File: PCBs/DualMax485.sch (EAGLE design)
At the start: 10 parts, among them IC2 7805DT, J1 6V-12V

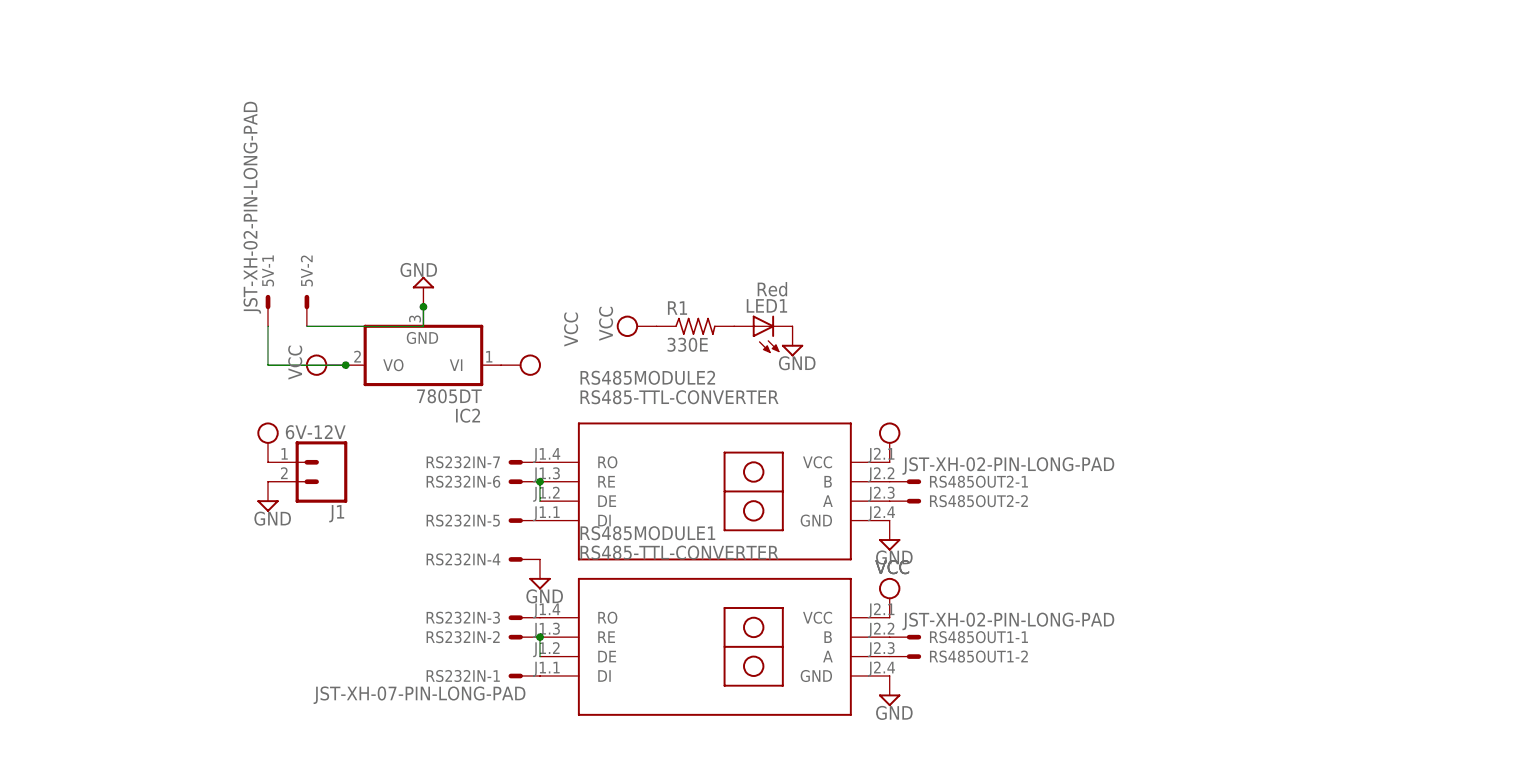
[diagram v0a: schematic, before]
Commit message: resistors added to max485
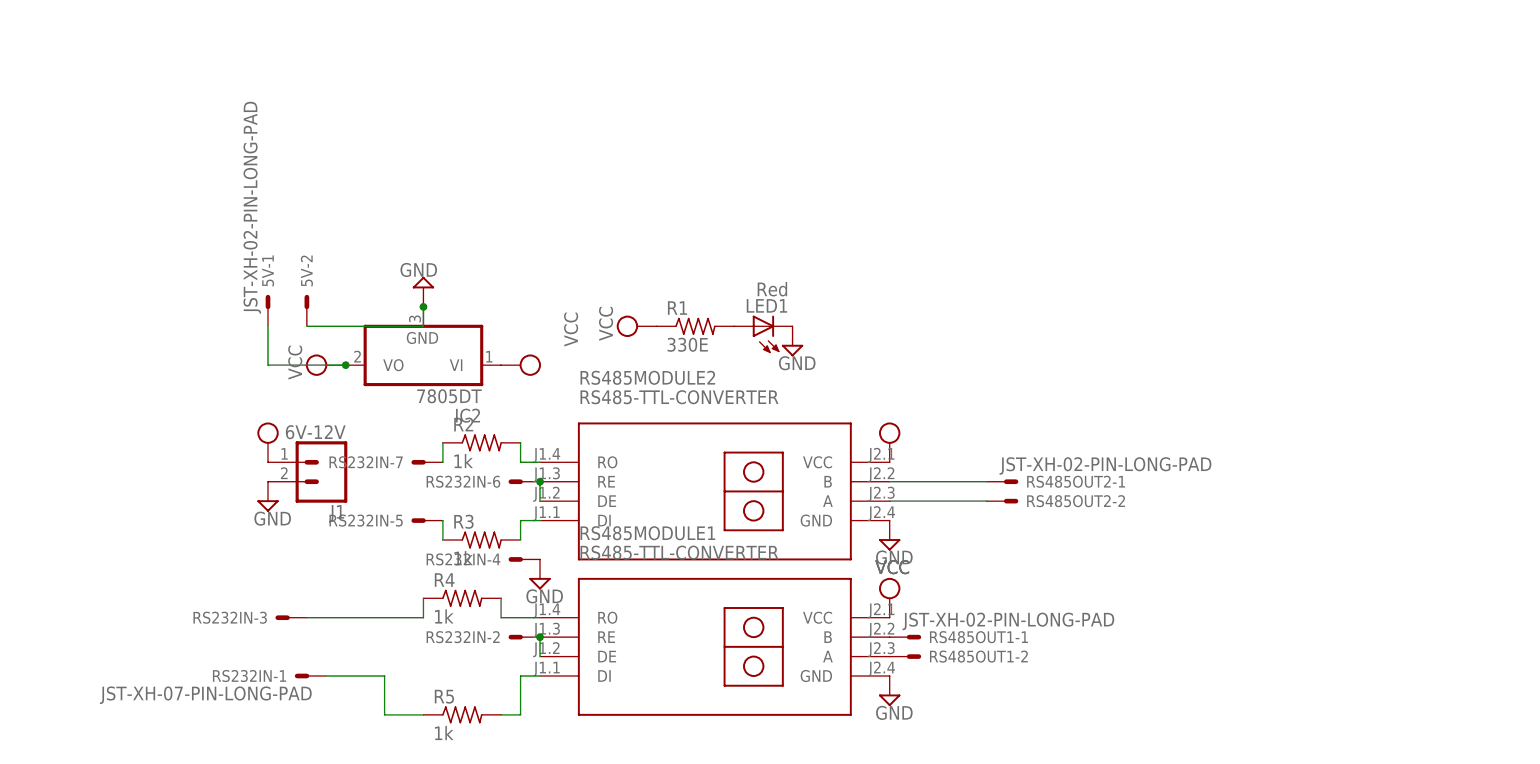
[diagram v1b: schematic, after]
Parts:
- added R2, R3, R4, R5: 1k, adafruit:R-US_M0805
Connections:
- new net N$11: R2.1, RS232IN-7.S
- new net N$14: R4.2, RS485MODULE1.RO
- new net N$15: R5.2, RS485MODULE1.DI
- new net N$5: R3.1, RS232IN-5.S
- net N$10: now also R4.1; no longer RS485MODULE1.RO
- net N$2: now also R3.2; no longer RS232IN-5.S
- net N$3: now also R2.2; no longer RS232IN-7.S
- net N$8: now also R5.1; no longer RS485MODULE1.DI
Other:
- moved on the sheet: RS232IN-1, RS232IN-3, RS232IN-5, RS232IN-7, RS485OUT2-1, RS485OUT2-2
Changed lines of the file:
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@@
 <part name="RS485MODULE1" library="diy-modules" deviceset="RS485-TTL-CONVERTER" device=""/>
 <part name="5V" library="Rembrandt Electronics - JST XH Connectors v1-0" deviceset="JST-XH-02-PIN" device="-LONG-PAD"/>
+<part name="R2" library="adafruit" deviceset="R-US_" device="M0805" value="1k"/>
+<part name="R3" library="adafruit" deviceset="R-US_" device="M0805" value="1k"/>
+<part name="R4" library="adafruit" deviceset="R-US_" device="M0805" value="1k"/>
+<part name="R5" library="adafruit" deviceset="R-US_" device="M0805" value="1k"/>
 </parts>
 <sheets>
@@
 <attribute name="VALUE" x="-37.465" y="116.205" size="1.778" layer="96"/>
 </instance>
-<instance part="RS232IN" gate="-1" x="-71.12" y="76.2" smashed="yes" rot="R180">
-<attribute name="NAME" x="-73.66" y="76.962" size="1.524" layer="95" rot="R180"/>
-<attribute name="VALUE" x="-70.358" y="74.803" size="1.778" layer="96" rot="R180"/>
+<instance part="RS232IN" gate="-1" x="-99.06" y="76.2" smashed="yes" rot="R180">
+<attribute name="NAME" x="-101.6" y="76.962" size="1.524" layer="95" rot="R180"/>
+<attribute name="VALUE" x="-98.298" y="74.803" size="1.778" layer="96" rot="R180"/>
 </instance>
 <instance part="RS232IN" gate="-2" x="-71.12" y="81.28" smashed="yes" rot="R180">
 <attribute name="NAME" x="-73.66" y="82.042" size="1.524" layer="95" rot="R180"/>
 </instance>
-<instance part="RS232IN" gate="-3" x="-71.12" y="83.82" smashed="yes" rot="R180">
-<attribute name="NAME" x="-73.66" y="84.582" size="1.524" layer="95" rot="R180"/>
+<instance part="RS232IN" gate="-3" x="-101.6" y="83.82" smashed="yes" rot="R180">
+<attribute name="NAME" x="-104.14" y="84.582" size="1.524" layer="95" rot="R180"/>
 </instance>
 <instance part="RS232IN" gate="-4" x="-71.12" y="91.44" smashed="yes" rot="R180">
 <attribute name="NAME" x="-73.66" y="92.202" size="1.524" layer="95" rot="R180"/>
 </instance>
-<instance part="RS232IN" gate="-5" x="-71.12" y="96.52" smashed="yes" rot="R180">
-<attribute name="NAME" x="-73.66" y="97.282" size="1.524" layer="95" rot="R180"/>
+<instance part="RS232IN" gate="-5" x="-83.82" y="96.52" smashed="yes" rot="R180">
+<attribute name="NAME" x="-86.36" y="97.282" size="1.524" layer="95" rot="R180"/>
 </instance>
 <instance part="RS232IN" gate="-6" x="-71.12" y="101.6" smashed="yes" rot="R180">
 <attribute name="NAME" x="-73.66" y="102.362" size="1.524" layer="95" rot="R180"/>
 </instance>
-<instance part="RS232IN" gate="-7" x="-71.12" y="104.14" smashed="yes" rot="R180">
-<attribute name="NAME" x="-73.66" y="104.902" size="1.524" layer="95" rot="R180"/>
+<instance part="RS232IN" gate="-7" x="-83.82" y="104.14" smashed="yes" rot="R180">
+<attribute name="NAME" x="-86.36" y="104.902" size="1.524" layer="95" rot="R180"/>
 </instance>
 <instance part="SUPPLY17" gate="GND" x="-68.58" y="88.9" smashed="yes">
@@
 <attribute name="VALUE" x="-21.082" y="82.677" size="1.778" layer="96"/>
 </instance>
-<instance part="RS485OUT2" gate="-2" x="-20.32" y="99.06" smashed="yes">
-<attribute name="NAME" x="-17.78" y="98.298" size="1.524" layer="95"/>
-</instance>
-<instance part="RS485OUT2" gate="-1" x="-20.32" y="101.6" smashed="yes">
-<attribute name="NAME" x="-17.78" y="100.838" size="1.524" layer="95"/>
-<attribute name="VALUE" x="-21.082" y="102.997" size="1.778" layer="96"/>
+<instance part="RS485OUT2" gate="-2" x="-7.62" y="99.06" smashed="yes">
+<attribute name="NAME" x="-5.08" y="98.298" size="1.524" layer="95"/>
+</instance>
+<instance part="RS485OUT2" gate="-1" x="-7.62" y="101.6" smashed="yes">
+<attribute name="NAME" x="-5.08" y="100.838" size="1.524" layer="95"/>
+<attribute name="VALUE" x="-8.382" y="102.997" size="1.778" layer="96"/>
 </instance>
 <instance part="IC2" gate="A1" x="-83.82" y="116.84" smashed="yes" rot="R180">
@@
 <attribute name="NAME" x="-103.378" y="127" size="1.524" layer="95" rot="R90"/>
 <attribute name="VALUE" x="-105.537" y="123.698" size="1.778" layer="96" rot="R90"/>
+</instance>
+<instance part="R2" gate="G$1" x="-76.2" y="106.68" smashed="yes">
+<attribute name="NAME" x="-80.01" y="108.1786" size="1.778" layer="95"/>
+<attribute name="VALUE" x="-80.01" y="103.378" size="1.778" layer="96"/>
+</instance>
+<instance part="R3" gate="G$1" x="-76.2" y="93.98" smashed="yes">
+<attribute name="NAME" x="-80.01" y="95.4786" size="1.778" layer="95"/>
+<attribute name="VALUE" x="-80.01" y="90.678" size="1.778" layer="96"/>
+</instance>
+<instance part="R4" gate="G$1" x="-78.74" y="86.36" smashed="yes">
+<attribute name="NAME" x="-82.55" y="87.8586" size="1.778" layer="95"/>
+<attribute name="VALUE" x="-82.55" y="83.058" size="1.778" layer="96"/>
+</instance>
+<instance part="R5" gate="G$1" x="-78.74" y="71.12" smashed="yes">
+<attribute name="NAME" x="-82.55" y="72.6186" size="1.778" layer="95"/>
+<attribute name="VALUE" x="-82.55" y="67.818" size="1.778" layer="96"/>
 </instance>
 </instances>
@@
 <net name="N$2" class="0">
 <segment>
-<pinref part="RS232IN" gate="-5" pin="S"/>
 <pinref part="RS485MODULE2" gate="G$1" pin="DI"/>
+<pinref part="R3" gate="G$1" pin="2"/>
+<wire x1="-71.12" y1="96.52" x2="-68.58" y2="96.52" width="0.1524" layer="91"/>
+<wire x1="-71.12" y1="96.52" x2="-71.12" y2="93.98" width="0.1524" layer="91"/>
 </segment>
 </net>
 <net name="N$3" class="0">
 <segment>
-<pinref part="RS232IN" gate="-7" pin="S"/>
 <pinref part="RS485MODULE2" gate="G$1" pin="RO"/>
+<wire x1="-71.12" y1="104.14" x2="-68.58" y2="104.14" width="0.1524" layer="91"/>
+<pinref part="R2" gate="G$1" pin="2"/>
+<wire x1="-71.12" y1="106.68" x2="-71.12" y2="104.14" width="0.1524" layer="91"/>
 </segment>
 </net>
@@
 <pinref part="RS485MODULE2" gate="G$1" pin="B"/>
 <pinref part="RS485OUT2" gate="-1" pin="S"/>
+<wire x1="-10.16" y1="101.6" x2="-22.86" y2="101.6" width="0.1524" layer="91"/>
 </segment>
 </net>
@@
 <pinref part="RS485MODULE2" gate="G$1" pin="A"/>
 <pinref part="RS485OUT2" gate="-2" pin="S"/>
+<wire x1="-10.16" y1="99.06" x2="-22.86" y2="99.06" width="0.1524" layer="91"/>
 </segment>
 </net>
@@
 <segment>
 <pinref part="RS232IN" gate="-1" pin="S"/>
-<pinref part="RS485MODULE1" gate="G$1" pin="DI"/>
+<wire x1="-96.52" y1="76.2" x2="-88.9" y2="76.2" width="0.1524" layer="91"/>
+<pinref part="R5" gate="G$1" pin="1"/>
+<wire x1="-83.82" y1="71.12" x2="-88.9" y2="71.12" width="0.1524" layer="91"/>
+<wire x1="-88.9" y1="71.12" x2="-88.9" y2="76.2" width="0.1524" layer="91"/>
 </segment>
 </net>
@@
 <segment>
 <pinref part="RS232IN" gate="-3" pin="S"/>
-<pinref part="RS485MODULE1" gate="G$1" pin="RO"/>
+<wire x1="-99.06" y1="83.82" x2="-83.82" y2="83.82" width="0.1524" layer="91"/>
+<pinref part="R4" gate="G$1" pin="1"/>
+<wire x1="-83.82" y1="86.36" x2="-83.82" y2="83.82" width="0.1524" layer="91"/>
 </segment>
 </net>
@@
 </segment>
 </net>
+<net name="N$5" class="0">
+<segment>
+<pinref part="R3" gate="G$1" pin="1"/>
+<pinref part="RS232IN" gate="-5" pin="S"/>
+<wire x1="-81.28" y1="96.52" x2="-81.28" y2="93.98" width="0.1524" layer="91"/>
+</segment>
+</net>
+<net name="N$11" class="0">
+<segment>
+<pinref part="RS232IN" gate="-7" pin="S"/>
+<pinref part="R2" gate="G$1" pin="1"/>
+<wire x1="-81.28" y1="106.68" x2="-81.28" y2="104.14" width="0.1524" layer="91"/>
+</segment>
+</net>
+<net name="N$15" class="0">
+<segment>
+<pinref part="RS485MODULE1" gate="G$1" pin="DI"/>
+<wire x1="-71.12" y1="76.2" x2="-68.58" y2="76.2" width="0.1524" layer="91"/>
+<pinref part="R5" gate="G$1" pin="2"/>
+<wire x1="-73.66" y1="71.12" x2="-71.12" y2="71.12" width="0.1524" layer="91"/>
+<wire x1="-71.12" y1="71.12" x2="-71.12" y2="76.2" width="0.1524" layer="91"/>
+</segment>
+</net>
+<net name="N$14" class="0">
+<segment>
+<pinref part="RS485MODULE1" gate="G$1" pin="RO"/>
+<wire x1="-73.66" y1="83.82" x2="-68.58" y2="83.82" width="0.1524" layer="91"/>
+<pinref part="R4" gate="G$1" pin="2"/>
+<wire x1="-73.66" y1="86.36" x2="-73.66" y2="83.82" width="0.1524" layer="91"/>
+</segment>
+</net>

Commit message: updated board
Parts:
- removed RS485OUT1, RS485OUT2: JST-XH-02-PIN-LONG-PAD, Rembrandt Electronics - JST XH Connectors v1-0:JST-XH-02-PIN-LONG-PAD
- added RS485CONNECTEDTOD-D+GND, RS485OUTCONNECTEDTOD-D+GND: JST-XH-03-PIN-LONG-PAD, Rembrandt Electronics - JST XH Connectors v1-0:JST-XH-03-PIN-LONG-PAD
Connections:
- net GND: now also RS485CONNECTEDTOD-D+GND-3.S, RS485OUTCONNECTEDTOD-D+GND-3.S
- net N$12: now also RS485CONNECTEDTOD-D+GND-1.S; no longer RS485OUT1-1.S
- net N$13: now also RS485CONNECTEDTOD-D+GND-2.S; no longer RS485OUT1-2.S
- net N$4: now also RS485OUTCONNECTEDTOD-D+GND-1.S; no longer RS485OUT2-1.S
- net N$6: now also RS485OUTCONNECTEDTOD-D+GND-2.S; no longer RS485OUT2-2.S
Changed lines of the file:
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@@
 <part name="RS232IN" library="Rembrandt Electronics - JST XH Connectors v1-0" deviceset="JST-XH-07-PIN" device="-LONG-PAD"/>
 <part name="SUPPLY17" library="supply2" library_urn="urn:adsk.eagle:library:372" deviceset="GND" device=""/>
-<part name="RS485OUT1" library="Rembrandt Electronics - JST XH Connectors v1-0" deviceset="JST-XH-02-PIN" device="-LONG-PAD"/>
-<part name="RS485OUT2" library="Rembrandt Electronics - JST XH Connectors v1-0" deviceset="JST-XH-02-PIN" device="-LONG-PAD"/>
 <part name="IC2" library="adafruit" deviceset="78*" device="DT" technology="05"/>
 <part name="RS485MODULE2" library="diy-modules" deviceset="RS485-TTL-CONVERTER" device=""/>
@@
 <part name="R4" library="adafruit" deviceset="R-US_" device="M0805" value="1k"/>
 <part name="R5" library="adafruit" deviceset="R-US_" device="M0805" value="1k"/>
+<part name="RS485OUTCONNECTEDTOD-D+GND" library="Rembrandt Electronics - JST XH Connectors v1-0" deviceset="JST-XH-03-PIN" device="-LONG-PAD"/>
+<part name="RS485CONNECTEDTOD-D+GND" library="Rembrandt Electronics - JST XH Connectors v1-0" deviceset="JST-XH-03-PIN" device="-LONG-PAD"/>
 </parts>
 <sheets>
@@
 <attribute name="VALUE" x="-24.765" y="89.535" size="1.778" layer="96"/>
 </instance>
-<instance part="SUPPLY6" gate="GND" x="-22.86" y="73.66" smashed="yes">
-<attribute name="VALUE" x="-24.765" y="70.485" size="1.778" layer="96"/>
+<instance part="SUPPLY6" gate="GND" x="-17.78" y="73.66" smashed="yes">
+<attribute name="VALUE" x="-19.685" y="70.485" size="1.778" layer="96"/>
 </instance>
 <instance part="SUPPLY12" gate="GND" x="-83.82" y="127" smashed="yes" rot="R180">
@@
 <attribute name="VALUE" x="-24.765" y="89.535" size="1.778" layer="96"/>
 </instance>
-<instance part="SUPPLY3" gate="GND" x="-22.86" y="93.98" smashed="yes">
-<attribute name="VALUE" x="-24.765" y="90.805" size="1.778" layer="96"/>
+<instance part="SUPPLY3" gate="GND" x="-15.24" y="93.98" smashed="yes">
+<attribute name="VALUE" x="-17.145" y="90.805" size="1.778" layer="96"/>
 </instance>
 <instance part="SUPPLY1" gate="G$1" x="-96.52" y="116.84" smashed="yes" rot="R90">
@@
 <attribute name="VALUE" x="-70.485" y="85.725" size="1.778" layer="96"/>
 </instance>
-<instance part="RS485OUT1" gate="-2" x="-20.32" y="78.74" smashed="yes">
-<attribute name="NAME" x="-17.78" y="77.978" size="1.524" layer="95"/>
-</instance>
-<instance part="RS485OUT1" gate="-1" x="-20.32" y="81.28" smashed="yes">
-<attribute name="NAME" x="-17.78" y="80.518" size="1.524" layer="95"/>
-<attribute name="VALUE" x="-21.082" y="82.677" size="1.778" layer="96"/>
-</instance>
-<instance part="RS485OUT2" gate="-2" x="-7.62" y="99.06" smashed="yes">
-<attribute name="NAME" x="-5.08" y="98.298" size="1.524" layer="95"/>
-</instance>
-<instance part="RS485OUT2" gate="-1" x="-7.62" y="101.6" smashed="yes">
-<attribute name="NAME" x="-5.08" y="100.838" size="1.524" layer="95"/>
-<attribute name="VALUE" x="-8.382" y="102.997" size="1.778" layer="96"/>
-</instance>
 <instance part="IC2" gate="A1" x="-83.82" y="116.84" smashed="yes" rot="R180">
 <attribute name="NAME" x="-76.2" y="111.125" size="1.778" layer="95" rot="R180"/>
@@
 <attribute name="NAME" x="-82.55" y="72.6186" size="1.778" layer="95"/>
 <attribute name="VALUE" x="-82.55" y="67.818" size="1.778" layer="96"/>
+</instance>
+<instance part="RS485OUTCONNECTEDTOD-D+GND" gate="-1" x="15.24" y="101.6" smashed="yes">
+<attribute name="NAME" x="17.78" y="100.838" size="1.524" layer="95"/>
+<attribute name="VALUE" x="14.478" y="102.997" size="1.778" layer="96"/>
+</instance>
+<instance part="RS485OUTCONNECTEDTOD-D+GND" gate="-2" x="15.24" y="99.06" smashed="yes">
+<attribute name="NAME" x="17.78" y="98.298" size="1.524" layer="95"/>
+</instance>
+<instance part="RS485OUTCONNECTEDTOD-D+GND" gate="-3" x="15.24" y="96.52" smashed="yes">
+<attribute name="NAME" x="17.78" y="95.758" size="1.524" layer="95"/>
+</instance>
+<instance part="RS485CONNECTEDTOD-D+GND" gate="-1" x="15.24" y="83.82" smashed="yes">
+<attribute name="NAME" x="17.78" y="83.058" size="1.524" layer="95"/>
+<attribute name="VALUE" x="14.478" y="85.217" size="1.778" layer="96"/>
+</instance>
+<instance part="RS485CONNECTEDTOD-D+GND" gate="-2" x="15.24" y="81.28" smashed="yes">
+<attribute name="NAME" x="17.78" y="80.518" size="1.524" layer="95"/>
+</instance>
+<instance part="RS485CONNECTEDTOD-D+GND" gate="-3" x="15.24" y="78.74" smashed="yes">
+<attribute name="NAME" x="17.78" y="77.978" size="1.524" layer="95"/>
 </instance>
 </instances>
@@
 <pinref part="RS485MODULE2" gate="G$1" pin="GND"/>
 <pinref part="SUPPLY3" gate="GND" pin="GND"/>
+<pinref part="RS485OUTCONNECTEDTOD-D+GND" gate="-3" pin="S"/>
+<wire x1="-15.24" y1="96.52" x2="12.7" y2="96.52" width="0.1524" layer="91"/>
+<wire x1="-15.24" y1="96.52" x2="-22.86" y2="96.52" width="0.1524" layer="91"/>
 </segment>
 <segment>
 <pinref part="RS485MODULE1" gate="G$1" pin="GND"/>
 <pinref part="SUPPLY6" gate="GND" pin="GND"/>
+<wire x1="-17.78" y1="76.2" x2="-2.54" y2="76.2" width="0.1524" layer="91"/>
+<wire x1="-2.54" y1="76.2" x2="-2.54" y2="78.74" width="0.1524" layer="91"/>
+<pinref part="RS485CONNECTEDTOD-D+GND" gate="-3" pin="S"/>
+<wire x1="-2.54" y1="78.74" x2="12.7" y2="78.74" width="0.1524" layer="91"/>
+<wire x1="-17.78" y1="76.2" x2="-22.86" y2="76.2" width="0.1524" layer="91"/>
+<junction x="-17.78" y="76.2"/>
 </segment>
 </net>
@@
 <segment>
 <pinref part="RS485MODULE2" gate="G$1" pin="B"/>
-<pinref part="RS485OUT2" gate="-1" pin="S"/>
-<wire x1="-10.16" y1="101.6" x2="-22.86" y2="101.6" width="0.1524" layer="91"/>
+<wire x1="-22.86" y1="101.6" x2="12.7" y2="101.6" width="0.1524" layer="91"/>
+<pinref part="RS485OUTCONNECTEDTOD-D+GND" gate="-1" pin="S"/>
 </segment>
 </net>
@@
 <segment>
 <pinref part="RS485MODULE2" gate="G$1" pin="A"/>
-<pinref part="RS485OUT2" gate="-2" pin="S"/>
-<wire x1="-10.16" y1="99.06" x2="-22.86" y2="99.06" width="0.1524" layer="91"/>
+<pinref part="RS485OUTCONNECTEDTOD-D+GND" gate="-2" pin="S"/>
+<wire x1="-22.86" y1="99.06" x2="12.7" y2="99.06" width="0.1524" layer="91"/>
 </segment>
 </net>
@@
 <net name="N$12" class="0">
 <segment>
+<pinref part="RS485CONNECTEDTOD-D+GND" gate="-1" pin="S"/>
+<wire x1="-7.62" y1="83.82" x2="12.7" y2="83.82" width="0.1524" layer="91"/>
+<wire x1="-7.62" y1="81.28" x2="-7.62" y2="83.82" width="0.1524" layer="91"/>
 <pinref part="RS485MODULE1" gate="G$1" pin="B"/>
-<pinref part="RS485OUT1" gate="-1" pin="S"/>
+<wire x1="-22.86" y1="81.28" x2="-7.62" y2="81.28" width="0.1524" layer="91"/>
 </segment>
 </net>
@@
 <segment>
 <pinref part="RS485MODULE1" gate="G$1" pin="A"/>
-<pinref part="RS485OUT1" gate="-2" pin="S"/>
-</segment>
-</net>
+<wire x1="-22.86" y1="78.74" x2="-5.08" y2="78.74" width="0.1524" layer="91"/>
+<wire x1="-5.08" y1="78.74" x2="-5.08" y2="81.28" width="0.1524" layer="91"/>
+<pinref part="RS485CONNECTEDTOD-D+GND" gate="-2" pin="S"/>
+<wire x1="-5.08" y1="81.28" x2="12.7" y2="81.28" width="0.1524" layer="91"/>
+</segment>
+</net>

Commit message: board updated
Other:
- moved on the sheet: R3, RS232IN-5
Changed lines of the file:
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@@
 <attribute name="NAME" x="-73.66" y="92.202" size="1.524" layer="95" rot="R180"/>
 </instance>
-<instance part="RS232IN" gate="-5" x="-83.82" y="96.52" smashed="yes" rot="R180">
-<attribute name="NAME" x="-86.36" y="97.282" size="1.524" layer="95" rot="R180"/>
+<instance part="RS232IN" gate="-5" x="-86.36" y="96.52" smashed="yes" rot="R180">
+<attribute name="NAME" x="-88.9" y="97.282" size="1.524" layer="95" rot="R180"/>
 </instance>
 <instance part="RS232IN" gate="-6" x="-71.12" y="101.6" smashed="yes" rot="R180">
@@
 <attribute name="VALUE" x="-80.01" y="103.378" size="1.778" layer="96"/>
 </instance>
-<instance part="R3" gate="G$1" x="-76.2" y="93.98" smashed="yes">
-<attribute name="NAME" x="-80.01" y="95.4786" size="1.778" layer="95"/>
-<attribute name="VALUE" x="-80.01" y="90.678" size="1.778" layer="96"/>
+<instance part="R3" gate="G$1" x="-76.2" y="96.52" smashed="yes">
+<attribute name="NAME" x="-80.01" y="98.0186" size="1.778" layer="95"/>
+<attribute name="VALUE" x="-80.01" y="93.218" size="1.778" layer="96"/>
 </instance>
 <instance part="R4" gate="G$1" x="-78.74" y="86.36" smashed="yes">
@@
 <pinref part="R3" gate="G$1" pin="2"/>
 <wire x1="-71.12" y1="96.52" x2="-68.58" y2="96.52" width="0.1524" layer="91"/>
-<wire x1="-71.12" y1="96.52" x2="-71.12" y2="93.98" width="0.1524" layer="91"/>
 </segment>
 </net>
@@
 <pinref part="R3" gate="G$1" pin="1"/>
 <pinref part="RS232IN" gate="-5" pin="S"/>
-<wire x1="-81.28" y1="96.52" x2="-81.28" y2="93.98" width="0.1524" layer="91"/>
-</segment>
-</net>
+<wire x1="-83.82" y1="96.52" x2="-81.28" y2="96.52" width="0.1524" layer="91"/>
+</segment>
+</net>
